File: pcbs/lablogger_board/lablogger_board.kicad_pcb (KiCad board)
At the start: 2 copper layers, 72 x 44 mm, 41 parts, among them J1 RJ45, J2 Conn_01x07, J3 Conn_01x12, J4 PINHD-1X4, P1 24V / 5A, Q1 220mA / 50V, Q2 220mA / 50V, Q3 220mA / 50V, Q4 220mA / 50V, U1 8-28V in / 5V 5W out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

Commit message: lablogger first version
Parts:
- removed J1: RJ45, footprints:RJ45_A-2014-2-4-N-T-R
- removed R18: 10kΩ, footprints:R_1206
- removed the R4 at (115.0, 121.0)
- removed the R5 at (148.5, 109.7)
- added C2: 100nF, footprints:C_0603, F.Cu at (153.5, 104.0)
- added C3: 100nF, footprints:C_0603, F.Cu at (142.0, 108.0)
- added C4: 100nF, footprints:C_0603, F.Cu at (142.0, 110.0)
- added C5: 100nF, footprints:C_0603, F.Cu at (145.5, 107.0)
- added C6: 100nF, footprints:C_0603, F.Cu at (145.5, 110.0)
- added J10: 5mm, footprints:TERMINAL_BLOCK_1x03_5mm_vertical, B.Cu at (124.5, 119.0)
- added J11: DB9, footprints:DB9_male, B.Cu at (150.5, 119.9)
- added J12: DB9, footprints:DB9_male, B.Cu at (150.5, 101.1)
- added J5: 5mm, footprints:TERMINAL_BLOCK_1x02_5mm_vertical, B.Cu at (109.0, 92.0)
- added J6: 5mm, footprints:TERMINAL_BLOCK_1x02_5mm_vertical, B.Cu at (124.5, 92.0)
- added J7: RJ11, footprints:RJ11_MOLEX_955032641, B.Cu at (163.7, 92.2)
- added J8: RJ11, footprints:RJ11_MOLEX_955032641, B.Cu at (163.7, 108.7)
- added J9: 5mm, footprints:TERMINAL_BLOCK_1x03_5mm_vertical, B.Cu at (102.5, 115.0)
- added R15: 120Ω, footprints:R_1206, F.Cu at (117.1, 122.2)
- added U3: RS485 Transceiver, footprints:8-SOIC, F.Cu at (154.2, 96.9)
- added U4: RS232 Transceiver, footprints:TSSOP16_MXL, F.Cu at (151.4, 108.3)
- C1: value 10nF -> 100nF; moved to F.Cu
- D1: value 3A/60V/750mV -> 1A/40V/500mV; footprint footprints:D_DO-214AB_SMC -> footprints:D_DO-214AC_SMA; moved to F.Cu
- D2: value 1A/40V/500mV -> 3A/60V/750mV; footprint footprints:D_DO-214AC_SMA -> footprints:D_DO-214AB_SMC; moved to F.Cu
- D3: value 40V -> 3A/60V/750mV; footprint footprints:D_DO-214AA_SMB -> footprints:D_DO-214AB_SMC; moved to F.Cu
- F1: value 33V/750mA/1.5A -> 24V/2.6A; footprint footprints:Fuse_1812 -> footprints:Fuse_2920_7451; moved to F.Cu
- Q1, Q2: value 220mA / 50V -> 5.7A / 30V; moved to F.Cu
- Q3, Q4, R1, R11, R12, R13, R14, R2, R7, R9, U1: moved to F.Cu
- R10: value 10kΩ -> 4.7kΩ; moved to F.Cu
- R3: value 100kΩ -> 10kΩ; moved to F.Cu
- R4: renamed from R17; moved to F.Cu
- R5: renamed from R16; moved to F.Cu
- R6: value 150Ω -> 100Ω; moved to F.Cu
- R8: value 1kΩ -> 100Ω; moved to F.Cu
- moved R10 50.7 mm to (107.0, 107.5), turned to -90 degrees
- moved R3 47.7 mm to (164.5, 102.5)
- moved Q1 42.2 mm to (114.0, 90.0), turned to 0 degrees
- moved R7 30.8 mm to (130.0, 109.0), turned to -90 degrees
- moved Q2 30.0 mm to (124.5, 88.0), turned to 180 degrees
- moved C1 28.7 mm to (153.5, 101.5)
- moved R11 26.1 mm to (167.5, 95.5), turned to 0 degrees
- moved R4 25.0 mm to (146.0, 87.5), turned to -90 degrees
- moved R6 21.6 mm to (133.0, 108.0)
- moved F1 21.1 mm to (126.1, 103.3)
- moved R13 21.1 mm to (167.5, 93.0), turned to 0 degrees
- moved R5 20.3 mm to (149.5, 87.5), turned to -90 degrees
- moved R9 15.7 mm to (136.0, 108.0)
- moved D1 15.0 mm to (133.0, 89.0)
- moved R1 14.1 mm to (126.0, 109.0), turned to -90 degrees
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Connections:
- net /A2-MOTOR renamed /A2-Switch1
- C1 pad 1: /A1-SIGNAL -> +3V3
- D1 pad 1: +24V -> +5V
- D1 pad 2: Net-(D1-A) -> +5Vout
- D2 pad 1: +5V -> +24V
- D2 pad 2: +5Vout -> Net-(D2-A)
- D3 pad 2: GND -> Net-(D3-A)
- F1 pad 1: Net-(D1-A) -> +24V
- J3 pad 1: GND -> +3V3
- J3 pad 10: +5V -> /D16-RX
- J3 pad 11: +24V -> /RX
- J3 pad 12: GND -> /TX
- J3 pad 2: /A0-VIN -> GND
- J3 pad 3: /A1-SIGNAL -> /A1
- J3 pad 5: /A5 -> /A5-Switch2
- J3 pad 6: /D6-DECO -> /S4
- J3 pad 7: /D1-SCL -> /S3
- J3 pad 8: /D0-SDA -> /D17-1Wire
- J3 pad 9: +3V3 -> /D15-TX
- Q1 pad 2: /5V-SPEED -> GND
- Q1 pad 3: Net-(Q1-D) -> Net-(D2-A)
- Q2 pad 1: +3V3 -> Net-(Q2-G)
- Q2 pad 2: /D6-DECO -> GND
- Q2 pad 3: /5V-DECO -> Net-(D3-A)
- R10 pad 1: /D6-DECO -> +3V3
- R10 pad 2: +3V3 -> /D17-1Wire
- R3 pad 1: /A1-SIGNAL -> +5Vout
- R7 pad 1: +5Vout -> Net-(Q1-G)
- R8 pad 1: +5V -> /A5-Switch2
- R8 pad 2: Net-(Q1-D) -> Net-(Q2-G)
- R9 pad 1: +5V -> Net-(Q2-G)
- R9 pad 2: /5V-DECO -> GND
- U2 pad 11: /SCK -> /D17-1Wire
- U2 pad 12: /MOSI -> /D15-TX
- U2 pad 13: /MISO -> /D16-RX
- U2 pad 21: /D4 -> /D4-TX
- U2 pad 22: /D5 -> /D5-RX
- U2 pad 23: /D6-DECO -> /D6
- U2 pad 24: /D7 -> /D7-RTS
- U2 pad 6: /A1-SIGNAL -> /A1
- U2 pad 8: /A5 -> /A5-Switch2
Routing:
- net +5V: track 134.2 -> 31.3 mm
- net +24V: track 139.4 -> 56.7 mm
- net /RS485-B: track 0.00 -> 76.2 mm, vias 0 -> 1
- net /RS485-A: track 0.00 -> 75.4 mm, vias 0 -> 1
- net /D6-DECO: track 74.8 -> 0.00 mm
- net /D17-1Wire: track 0.00 -> 59.4 mm
- net GND: track 262.5 -> 316.9 mm
- net +5Vout: track 67.7 -> 116.8 mm
- net +3V3: track 106.4 -> 150.0 mm
- net /TO-RS232 #1: track 0.00 -> 32.9 mm
- net Net-(Q1-G): track 8.96 -> 41.4 mm
- net /SIGNAL: track 32.0 -> 0.00 mm
- net /A2-Switch1: track 39.2 -> 8.06 mm
- net Net-(Q2-G): track 0.00 -> 28.6 mm
- net /5V-DECO: track 27.6 -> 0.00 mm
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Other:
- board text added: "#1 RS232"
- board text added: "#2 RS232"
- board text added: "1Wire"
- board text added: "I2C (3V3)"
- board text added: "I2C (5V)"
- board text added: "RS485"
- board text added: "Switch1"
- board text added: "Switch2"
- board text removed: "3V3"
- board text removed: "A0"
- board text removed: "A1"
- board text removed: "A2"
- board text removed: "A5"
- board text removed: "D0"
- board text removed: "D1"
- board text removed: "D6"
- board text removed: "DEC"
- board text removed: "GEOM.KOPFLAB.ORG"
- board text removed: "MOT"
- board text removed: "Photon2"
- board text removed: "SCL"
- board text removed: "SDA"
- board text removed: "SIG"
- board text removed: "VIN"

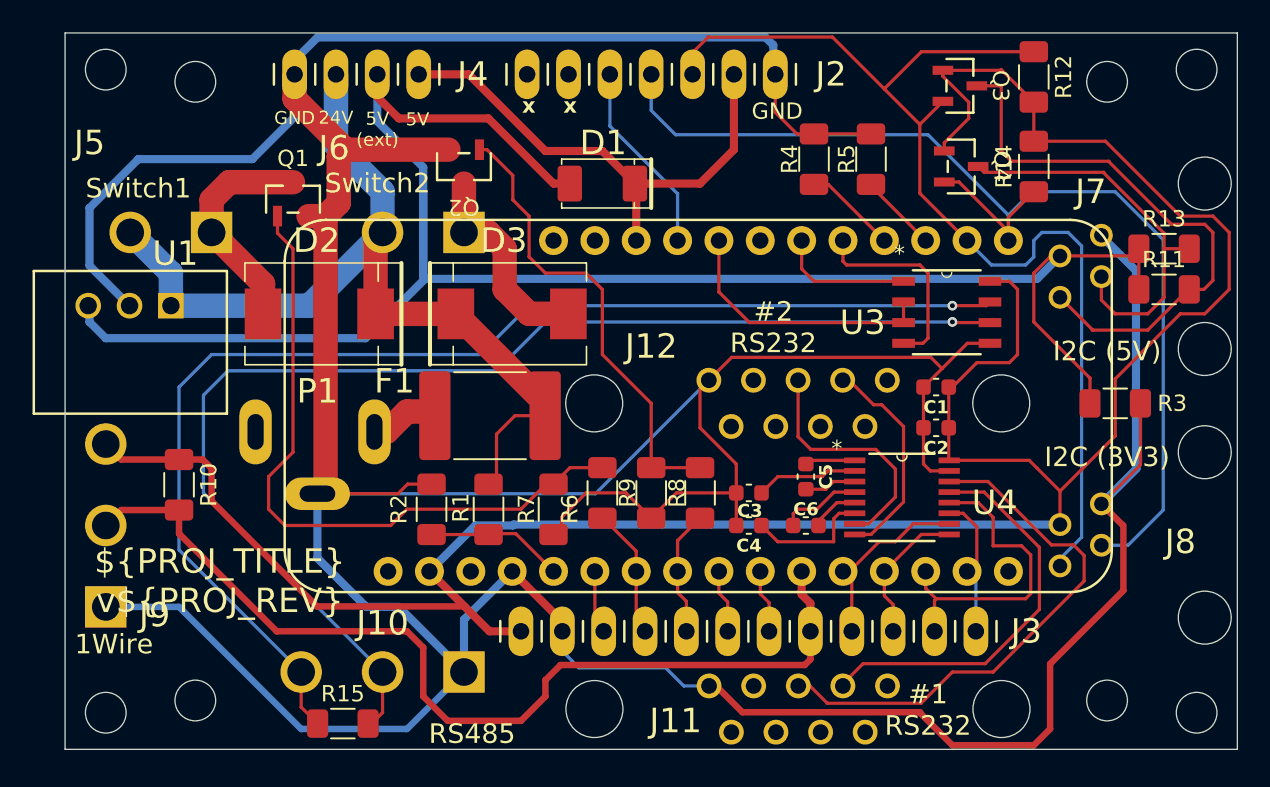
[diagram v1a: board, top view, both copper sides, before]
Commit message: update pcb to version 0.3: make holes for db9 connectors bigger
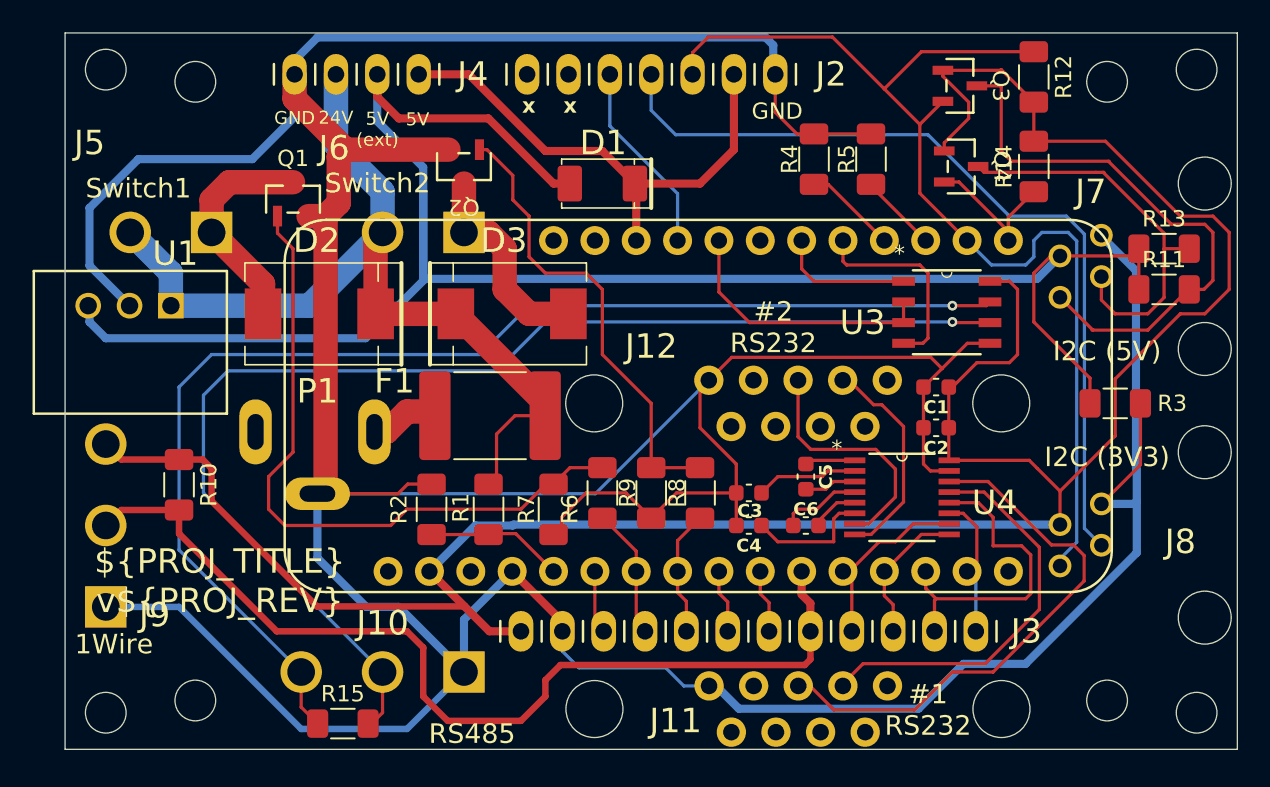
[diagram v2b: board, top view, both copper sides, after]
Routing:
- net /D0-SDA: track 70.4 -> 62.5 mm
- net GND: track 316.9 -> 312.9 mm
